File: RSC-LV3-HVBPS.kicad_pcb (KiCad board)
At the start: 2 copper layers, 140 x 85 mm, 100 parts, among them J1 FTSH-105-01-L-DV-K-A, J17 Molex 43045-0400, J18 Molex 43045-0400, J19 Molex 43045-0400, J2 USB_C_Receptacle_USB2.0_16P, J3 Molex 43650-0500, J4 Molex 43650-0500, J5 Molex 43650-0200, Q11 AO3400A, Q12 AO3400A, U1 STM32G0B1CBTx, U2 TPS54302, U3 TLV74033PDBVR, U4 TJA1051T-3, U5 TJA1051T-3, Y1 Crystal_GND24, Y2 32.768 kHz 6pF

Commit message: initial layout
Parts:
- added J20: Molex 43045-0400, Connector_Molex:Molex_Micro-Fit_3.0_43045-0412_2x02_P3.00mm_Vertical, F.Cu at (128.6, 96.1)
- added J5: Molex 43650-0200, Connector_Molex:Molex_Micro-Fit_3.0_43650-0215_1x02_P3.00mm_Vertical, F.Cu at (91.5, 97.5)
- added J6: Conn_01x04, Connector_Molex:Molex_KK-254_AE-6410-04A_1x04_P2.54mm_Vertical, F.Cu at (91.5, 104.0)
- added J7: Conn_01x04, Connector_Molex:Molex_KK-254_AE-6410-04A_1x04_P2.54mm_Vertical, F.Cu at (91.5, 115.5)
- added R70: 5.1k, Resistor_SMD:R_0603_1608Metric_Pad0.98x0.95mm_HandSolder, F.Cu at (106.8, 118.0)
- added R71: 5.1k, Resistor_SMD:R_0603_1608Metric_Pad0.98x0.95mm_HandSolder, F.Cu at (104.8, 118.0)
- J17, J18, J19: footprint Project_Library:Molex_Micro-Fit_3.0_43045-0400_2x02_P3.00mm_Horizontal_VerticalCompatible -> Connector_Molex:Molex_Micro-Fit_3.0_43045-0412_2x02_P3.00mm_Vertical
- J3, J4: footprint Project_Library:Molex_Micro-Fit_3.0_43650-0500_1x05_P3.00mm_Horizontal_VerticalCompatible -> Connector_Molex:Molex_Micro-Fit_3.0_43650-0515_1x05_P3.00mm_Vertical
- J5: footprint Project_Library:Molex_Micro-Fit_3.0_43650-0200_1x02_P3.00mm_Horizontal_VerticalCompatible -> Connector_Molex:Molex_Micro-Fit_3.0_43650-0215_1x02_P3.00mm_Vertical
- moved R69 91.2 mm to (108.1, 97.8), turned to 180 degrees
- moved J19 90.1 mm to (104.0, 86.0)
- moved R68 86.8 mm to (108.1, 99.8)
- moved R67 80.6 mm to (115.8, 102.1)
- moved J18 78.9 mm to (116.3, 86.0)
- moved D46 78.7 mm to (103.8, 98.8), turned to 90 degrees
- moved J5 76.3 mm to (154.5, 86.0), turned to 0 degrees
- moved R64 75.4 mm to (119.1, 99.3), turned to -90 degrees
- moved Q12 74.9 mm to (115.8, 99.1), turned to 90 degrees
- moved J17 74.6 mm to (128.6, 86.0)
- moved C39 73.9 mm to (105.6, 98.8), turned to 90 degrees
- moved R63 72.7 mm to (121.1, 99.3), turned to 90 degrees
- moved R66 71.3 mm to (126.6, 108.0), turned to 180 degrees
- moved S5 70.9 mm to (145.0, 88.0), turned to 180 degrees
- moved D44 67.9 mm to (138.4, 99.4), turned to 90 degrees
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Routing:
- net GND: track 359.2 -> 161.6 mm, vias 8 -> 4
- net NRST: track 123.2 -> 19.9 mm, vias 3 -> 2
- net BOOT0: track 107.3 -> 18.0 mm, vias 2 -> 1
- net +5V_USB: track 79.8 -> 0.00 mm
- net BTN_USR1: track 74.8 -> 6.52 mm, vias 2 -> 0
- net PRIMARY_CAN-: track 59.7 -> 0.00 mm, vias 2 -> 0
- net +5V_BUS: track 57.8 -> 0.00 mm, vias 2 -> 0
- net PRIMARY_CAN+: track 57.4 -> 0.00 mm, vias 3 -> 0
- net +12V_IN: track 59.1 -> 3.40 mm
- net STAT1_G: track 55.5 -> 0.00 mm, vias 2 -> 0
- net STAT0_G: track 53.3 -> 0.00 mm
- net STAT0_R: track 47.7 -> 0.00 mm
- net STAT1_B: track 52.2 -> 4.72 mm
- net STAT1_R: track 47.4 -> 2.23 mm, vias 2 -> 1
- net STAT0_B: track 41.0 -> 0.00 mm, vias 2 -> 0
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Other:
- board size 140 x 85 mm -> 124 x 53 mm
- board text added: "BMS PWR + DE"
- board text added: "E-STOP SWITCH"
- board text added: "FAN 1"
- board text added: "FAN 2"
- board text added: "LV3 HVBPS"
- board text added: "MAIN CONTACTORS"
- board text added: "MOD. LED"
- board text removed: "1"
- board text removed: "10"
- board text removed: "2"
- board text removed: "3"
- board text removed: "4"
- board text removed: "5"
- board text removed: "6"
- board text removed: "7"
- board text removed: "8"
- board text removed: "9"
- board text removed: "LV3 SwitchSense"

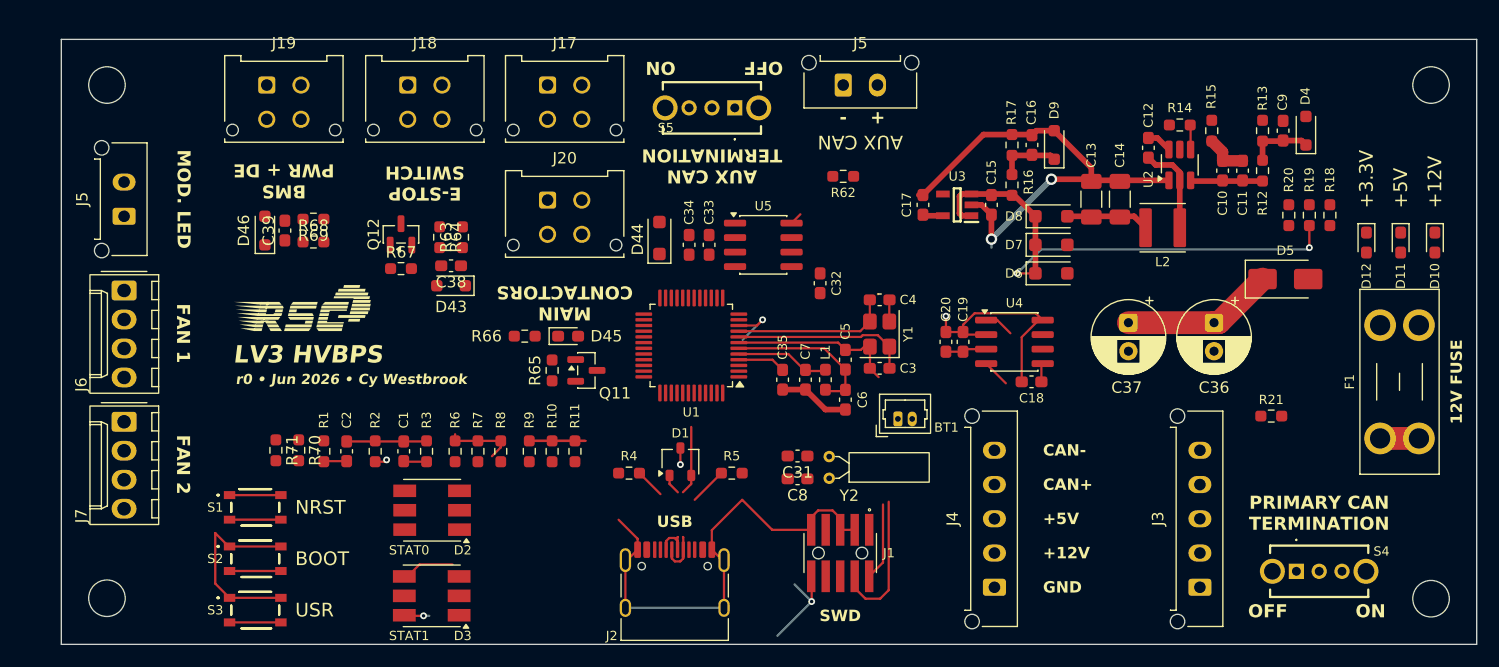
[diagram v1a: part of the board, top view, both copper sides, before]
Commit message: more layout and some initial routing
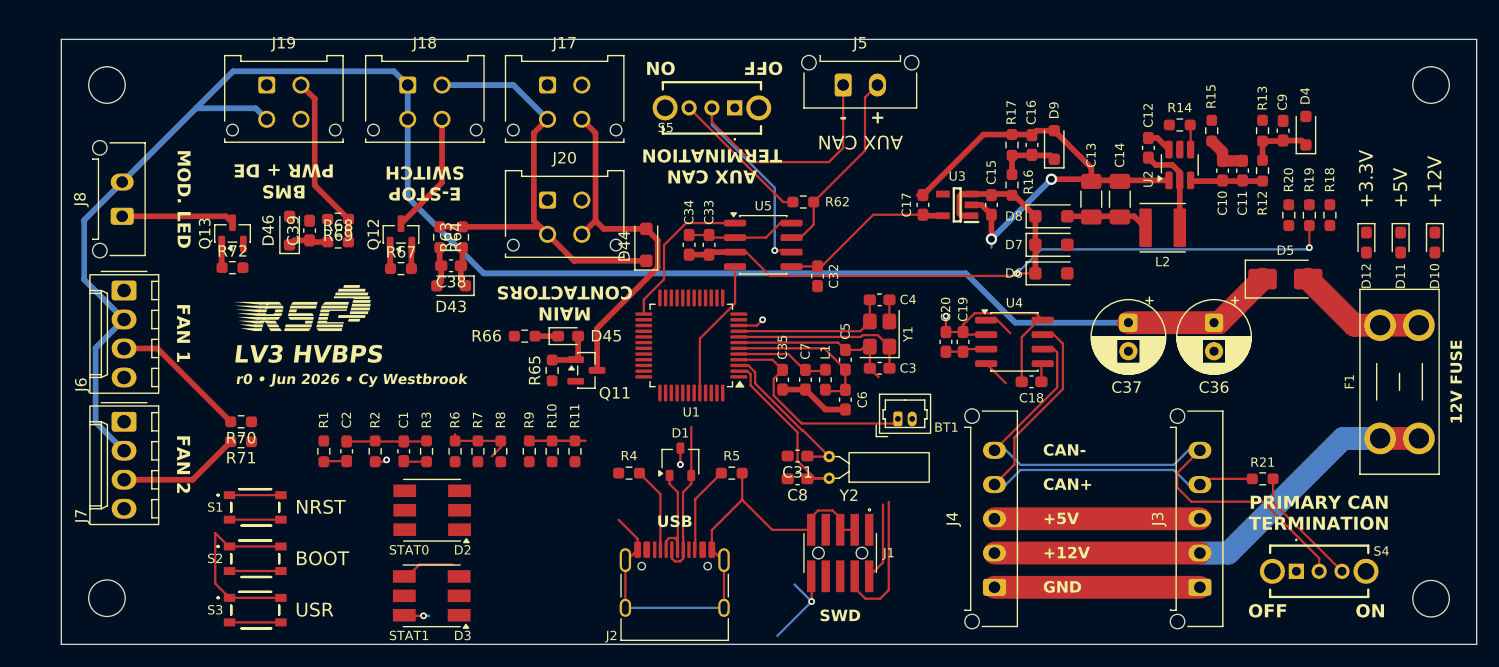
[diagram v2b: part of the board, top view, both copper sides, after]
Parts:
- removed the J5 at (91.5, 97.5)
- added J8: Molex 43650-0200, Connector_Molex:Molex_Micro-Fit_3.0_43650-0215_1x02_P3.00mm_Vertical, F.Cu at (91.3, 97.5)
- added Q13: AO3400A, Package_TO_SOT_SMD:SOT-23, F.Cu at (101.0, 99.0)
- added R72: 5.1k, Resistor_SMD:R_0603_1608Metric_Pad0.98x0.95mm_HandSolder, F.Cu at (101.0, 102.0)
- moved R70 5.63 mm to (101.8, 115.5), turned to 180 degrees
- moved R21 5.55 mm to (191.2, 120.5)
- moved R62 4.16 mm to (151.0, 96.2)
- moved R71 3.14 mm to (101.8, 117.2), turned to 180 degrees
- moved C39 2.16 mm to (107.8, 98.8)
- moved D46 2.16 mm to (106.0, 98.8)
- moved R68 2.16 mm to (110.2, 99.8)
- moved R69 2.16 mm to (110.2, 97.8)
- moved D44 1.30 mm to (137.2, 100.0)
- moved C32 0.65 mm to (152.2, 102.8)
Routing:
- net +12V: track 19.7 -> 161.9 mm
- net PRIMARY_CAN-: track 0.00 -> 51.5 mm
- net Net-(D44-K): track 0.00 -> 40.9 mm
- net PRIMARY_CAN+: track 0.00 -> 40.8 mm
- net +12V_IN: track 3.40 -> 41.3 mm
- net AUX_CAN-: track 0.00 -> 36.5 mm, vias 0 -> 1
- net GND: track 161.6 -> 196.1 mm
- net Net-(D44-A): track 0.00 -> 30.8 mm
- net +5V: track 48.9 -> 78.7 mm
- net +5V_BUS: track 0.00 -> 18.0 mm
- net AUX_CAN+: track 0.00 -> 16.9 mm
- net LSE_IN: track 0.00 -> 15.8 mm
- net Net-(J19-Pin_2): track 0.00 -> 15.5 mm
- net Net-(BT1-+): track 4.21 -> 18.8 mm
- net FDCAN2_TX: track 0.00 -> 13.8 mm
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
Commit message: full layout routing and silkscreen
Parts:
- moved R70 1.35 mm to (102.2, 116.8)
- moved R71 1.35 mm to (102.2, 118.5)
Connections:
- U1 pad 13: IN_1 -> E_STOP_SENSE
- U1 pad 14: IN_2 -> E_STOP_SWITCH_LED
- U1 pad 15: IN_3 -> MAIN_CONTACTOR_ENABLE
- U1 pad 16: IN_4 -> BMS_DE_SENSE
- U1 pad 17: IN_5 -> MODULE_LED
- U1 pad 18: IN_6 -> unconnected-(U1-PA7-Pad18)
- U1 pad 19: OUT_3 -> unconnected-(U1-PB0-Pad19)
- U1 pad 20: OUT_4 -> unconnected-(U1-PB1-Pad20)
- U1 pad 21: IN_7 -> unconnected-(U1-PB2-Pad21)
- U1 pad 22: IN_8 -> unconnected-(U1-PB10-Pad22)
- U1 pad 23: IN_9 -> unconnected-(U1-PB11-Pad23)
- U1 pad 24: IN_10 -> unconnected-(U1-PB12-Pad24)
- U1 pad 26: OUT_9 -> unconnected-(U1-PB14-Pad26)
- U1 pad 27: OUT_10 -> unconnected-(U1-PB15-Pad27)
- U1 pad 31: OUT_2 -> unconnected-(U1-PC7-Pad31)
- U1 pad 43: OUT_1 -> unconnected-(U1-PB4-Pad43)
- U1 pad 45: OUT_5 -> FAN_1_TACH
- U1 pad 46: OUT_6 -> FAN_1_PWM
- U1 pad 47: OUT_7 -> FAN_2_TACH
- U1 pad 48: OUT_8 -> FAN_2_PWM
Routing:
- net +3.3V: track 47.5 -> 212.1 mm, vias 0 -> 6
- net GND: track 196.1 -> 355.6 mm, vias 4 -> 6
- net +5V_USB: track 0.00 -> 75.5 mm
- net NRST: track 17.4 -> 84.0 mm
- net BOOT0: track 18.0 -> 76.5 mm, vias 1 -> 4
- net FAN_2_PWM: track 0.00 -> 58.1 mm
- net FAN_2_TACH: track 10.7 -> 67.2 mm, vias 0 -> 1
- net FAN_1_TACH: track 12.0 -> 68.0 mm, vias 0 -> 1
- net FAN_1_PWM: track 0.00 -> 54.8 mm
- net V_SENSE_12: track 5.66 -> 60.4 mm, vias 0 -> 2
- net BTN_USR1: track 6.52 -> 60.0 mm, vias 0 -> 2
- net MODULE_LED: track 2.08 -> 48.6 mm, vias 0 -> 2
- net BMS_DE_SENSE: track 3.55 -> 42.4 mm, vias 0 -> 2
- net E_STOP_SWITCH_LED: track 2.08 -> 36.0 mm, vias 0 -> 2
- net STAT1_G: track 0.00 -> 33.9 mm, vias 0 -> 2
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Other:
- board text added: "DE"
- board text added: "L+"
- board text added: "L-"
- board text added: "PWM"
- board text added: "SW"
- board text added: "TACH"

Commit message: r0 final
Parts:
- removed the D4 at (195.0, 90.0)
- removed the D9 at (173.0, 91.2)
- moved S4 0.50 mm to (194.2, 129.1)
- renumbered C38 to C1, C35 to C10, C6 to C11, C7 to C12, C9 to C13, C36 to C14, C37 to C15, C10 to C16, C11 to C17, C12 to C18, C13 to C19, C39 to C2, C14 to C20, C15 to C21, C16 to C22, C17 to C23, C18 to C24, C19 to C25, C20 to C26, C32 to C27, C33 to C28, C34 to C29, C1 to C3, C2 to C4, C3 to C5, C8 to C6, C4 to C7, C31 to C8, C5 to C9, D43 to D1, D7 to D10, D8 to D11, D10 to D12, D11 to D13, D12 to D14, D44 to D2, D45 to D3, D46 to D4, D1 to D5, D2 to D6, D3 to D7, D5 to D8, D6 to D9, J20 to J1, J3 to J10, J5 to J11, J4 to J12, J17 to J2, J18 to J3, J8 to J4, J19 to J5, J1 to J8, J2 to J9, Q11 to Q1, Q12 to Q2, Q13 to Q3, R63 to R1, R69 to R10, R1 to R11, R2 to R12, R3 to R13, R4 to R14, R5 to R15, R6 to R16, R7 to R17, R8 to R18, R9 to R19, R64 to R2, R10 to R20, R11 to R21, R12 to R22, R13 to R23, R14 to R24, R15 to R25, R16 to R26, R17 to R27, R18 to R28, R19 to R29, R65 to R3, R20 to R30, R21 to R31, R62 to R32, R66 to R4, R67 to R5, R70 to R6, R71 to R7, R68 to R8, R72 to R9
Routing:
- net GND: track 355.6 -> 419.4 mm
- net +5V_BUS: track 49.1 -> 67.1 mm
- net +12V_IN: track 41.3 -> 59.3 mm
- net V_SENSE_12: track 60.4 -> 58.2 mm
- net V_SENSE_5: track 34.8 -> 32.7 mm
- net Net-(D2-A): track 30.8 -> 31.4 mm
- net Net-(S4-NO): track 10.6 -> 11.1 mm
